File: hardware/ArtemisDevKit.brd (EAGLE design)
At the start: 94 x 38.1 mm, 228 parts, among them J2 CORTEX_JTAG_DEBUG_MINIMUM_PTH, J3 CORTEX_JTAG_DEBUG_PTH, J5 1X04_SMD_STRAIGHT_COMBO, J6 QWIIC_RIGHT_ANGLE, J7 CAMERA-HIMAX, J9 1X04_SMD_STRAIGHT_COMBO, U1 DAPLINK_KL26Z, U2 ARTEMIS_MODULESMD, U3 LIS2DH12, U4 AP2127K-1.8V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

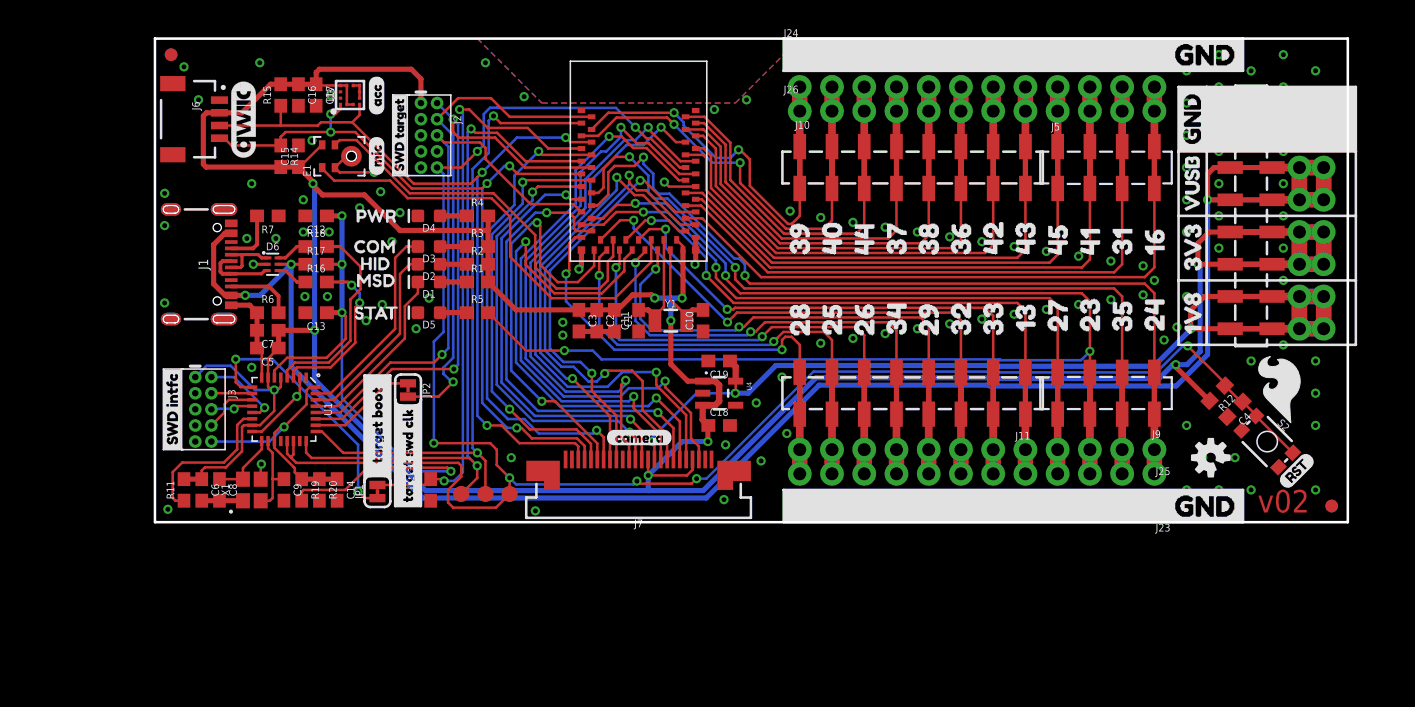
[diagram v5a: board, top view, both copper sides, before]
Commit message: final touches for review
- updated library in use for the interface chip
- mitered jumper labels
- approved / fixed all drc errors
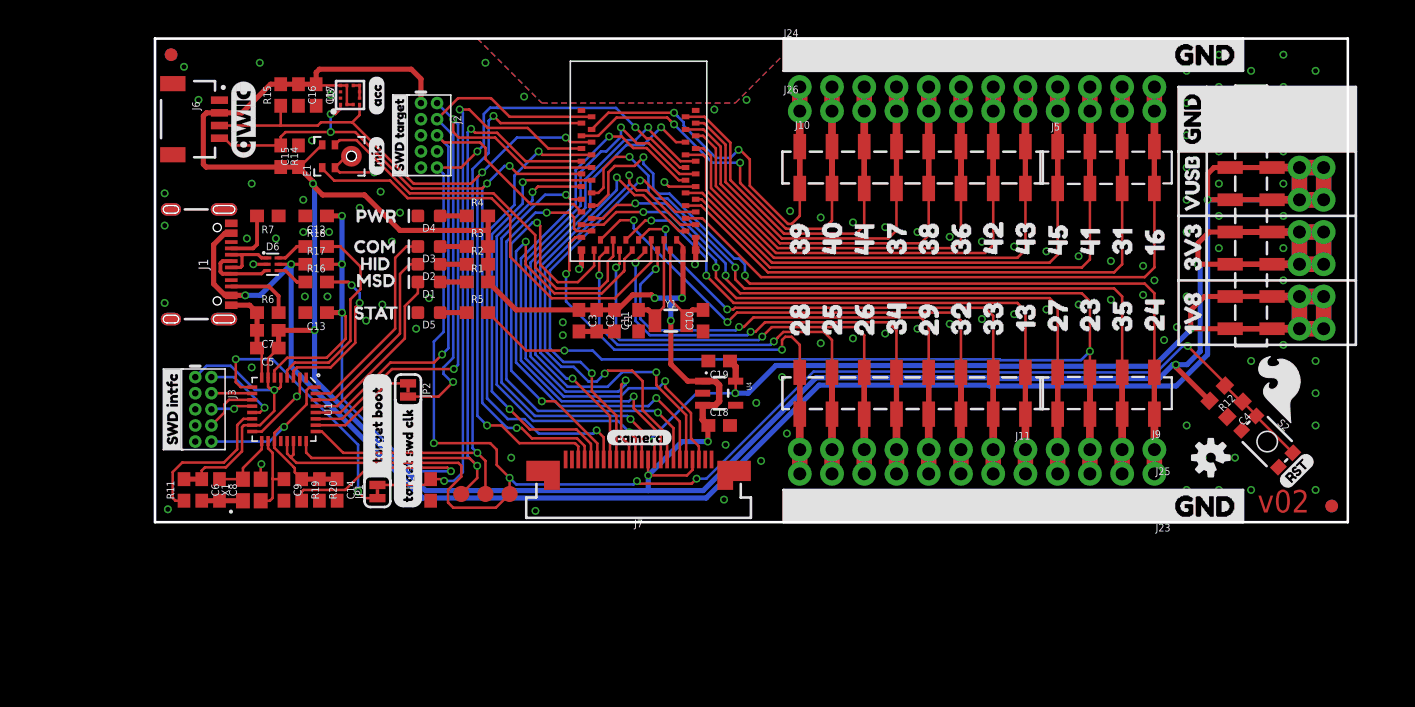
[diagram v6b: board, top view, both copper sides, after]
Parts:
- U1: device artembed:QFN-32-NOPAD -> ArtemisDevKit:QFN-32-NOPAD
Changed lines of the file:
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@@
 <layer number="37" name="tTest" color="7" fill="1" visible="no" active="yes"/>
 <layer number="38" name="bTest" color="7" fill="1" visible="no" active="yes"/>
-<layer number="39" name="tKeepout" color="4" fill="11" visible="no" active="yes"/>
-<layer number="40" name="bKeepout" color="1" fill="11" visible="no" active="yes"/>
+<layer number="39" name="tKeepout" color="4" fill="11" visible="yes" active="yes"/>
+<layer number="40" name="bKeepout" color="1" fill="11" visible="yes" active="yes"/>
 <layer number="41" name="tRestrict" color="4" fill="10" visible="no" active="yes"/>
 <layer number="42" name="bRestrict" color="1" fill="10" visible="no" active="yes"/>
@@
 <dimension x1="0" y1="38.1" x2="93.98" y2="38.1" x3="46.99" y3="44.45" textsize="1.778" textratio="15" layer="47" unit="inch"/>
 <text x="50.8" y="-13.335" size="1.778" layer="51" font="fixed" ratio="15">Owen Lyke, Kyle Wenner</text>
-<wire x1="16.51" y1="3.175" x2="16.51" y2="11.557" width="0.2032" layer="21"/>
-<wire x1="18.542" y1="11.557" x2="18.542" y2="2.921" width="0.2032" layer="21"/>
-<wire x1="18.542" y1="11.557" x2="16.51" y2="11.557" width="0.2032" layer="21"/>
-<wire x1="18.923" y1="9.652" x2="18.923" y2="1.27" width="0.2032" layer="21"/>
-<wire x1="18.923" y1="1.27" x2="20.955" y2="1.27" width="0.2032" layer="21"/>
-<wire x1="20.955" y1="1.27" x2="20.955" y2="9.652" width="0.2032" layer="21"/>
+<wire x1="17.145" y1="11.557" x2="17.907" y2="11.557" width="0.2032" layer="21"/>
+<wire x1="17.907" y1="11.557" x2="18.542" y2="10.922" width="0.2032" layer="21" curve="-90"/>
+<wire x1="18.542" y1="10.922" x2="18.542" y2="2.921" width="0.2032" layer="21"/>
+<wire x1="17.145" y1="11.557" x2="16.51" y2="10.922" width="0.2032" layer="21" curve="90"/>
+<wire x1="16.51" y1="10.922" x2="16.51" y2="3.175" width="0.2032" layer="21"/>
+<wire x1="18.923" y1="9.652" x2="18.923" y2="1.905" width="0.2032" layer="21"/>
+<wire x1="18.923" y1="1.905" x2="19.558" y2="1.27" width="0.2032" layer="21" curve="90"/>
+<wire x1="19.558" y1="1.27" x2="20.32" y2="1.27" width="0.2032" layer="21"/>
+<wire x1="20.32" y1="1.27" x2="20.955" y2="1.905" width="0.2032" layer="21" curve="90"/>
+<wire x1="20.955" y1="1.905" x2="20.955" y2="9.652" width="0.2032" layer="21"/>
 <rectangle x1="16.51" y1="4.191" x2="17.018" y2="10.922" layer="21"/>
 <rectangle x1="18.034" y1="4.191" x2="18.542" y2="10.922" layer="21"/>
-<rectangle x1="18.923" y1="1.27" x2="19.431" y2="9.271" layer="21"/>
-<rectangle x1="20.447" y1="1.27" x2="20.955" y2="9.271" layer="21"/>
 <rectangle x1="16.51" y1="3.556" x2="18.542" y2="4.445" layer="21"/>
-<rectangle x1="16.51" y1="10.795" x2="18.542" y2="11.557" layer="21"/>
+<rectangle x1="18.923" y1="1.524" x2="19.431" y2="9.271" layer="21"/>
+<rectangle x1="19.05" y1="1.397" x2="19.431" y2="1.651" layer="21"/>
+<rectangle x1="20.447" y1="1.397" x2="20.828" y2="1.651" layer="21"/>
+<rectangle x1="20.447" y1="1.524" x2="20.955" y2="9.271" layer="21"/>
+<rectangle x1="16.764" y1="10.795" x2="18.288" y2="11.557" layer="21"/>
+<rectangle x1="18.161" y1="10.922" x2="18.415" y2="11.43" layer="21"/>
+<rectangle x1="18.288" y1="10.795" x2="18.542" y2="11.303" layer="21"/>
+<rectangle x1="16.637" y1="10.795" x2="16.891" y2="11.43" layer="21"/>
+<rectangle x1="16.51" y1="10.795" x2="16.764" y2="11.176" layer="21"/>
 </plain>
 <attributes>
@@
 </class>
 </classes>
-<designrules name="SparkFun-2-layer-TIGHT">
+<designrules name="SparkFun-2-layer-FAB-LIMIT">
 <description language="en">&lt;b&gt;SparkFun 2 Layer Design Rule Checks - STANDARD/TIGHT/FAB-LIMIT&lt;/b&gt;
 &lt;p&gt;
@@
 <param name="mtCopper" value="0.035mm 0.035mm 0.035mm 0.035mm 0.035mm 0.035mm 0.035mm 0.035mm 0.035mm 0.035mm 0.035mm 0.035mm 0.035mm 0.035mm 0.035mm 0.035mm"/>
 <param name="mtIsolate" value="1.5mm 0.15mm 0.2mm 0.15mm 0.2mm 0.15mm 0.2mm 0.15mm 0.2mm 0.15mm 0.2mm 0.15mm 0.2mm 0.15mm 0.2mm"/>
-<param name="mdWireWire" value="7mil"/>
-<param name="mdWirePad" value="7mil"/>
-<param name="mdWireVia" value="7mil"/>
-<param name="mdPadPad" value="7mil"/>
-<param name="mdPadVia" value="7mil"/>
-<param name="mdViaVia" value="7mil"/>
-<param name="mdSmdPad" value="7mil"/>
-<param name="mdSmdVia" value="7mil"/>
-<param name="mdSmdSmd" value="7mil"/>
+<param name="mdWireWire" value="4mil"/>
+<param name="mdWirePad" value="4mil"/>
+<param name="mdWireVia" value="4mil"/>
+<param name="mdPadPad" value="4mil"/>
+<param name="mdPadVia" value="4mil"/>
+<param name="mdViaVia" value="4mil"/>
+<param name="mdSmdPad" value="4mil"/>
+<param name="mdSmdVia" value="4mil"/>
+<param name="mdSmdSmd" value="4mil"/>
 <param name="mdViaViaSameLayer" value="8mil"/>
 <param name="mnLayersViaInSmd" value="2"/>
-<param name="mdCopperDimension" value="7mil"/>
-<param name="mdDrill" value="7mil"/>
+<param name="mdCopperDimension" value="4mil"/>
+<param name="mdDrill" value="4mil"/>
 <param name="mdSmdStop" value="0mil"/>
-<param name="msWidth" value="7mil"/>
-<param name="msDrill" value="15mil"/>
+<param name="msWidth" value="4mil"/>
+<param name="msDrill" value="6mil"/>
 <param name="msMicroVia" value="9.99mm"/>
 <param name="msBlindViaRatio" value="0.5"/>
@@
 <param name="rvMicroViaOuter" value="0.25"/>
 <param name="rvMicroViaInner" value="0.25"/>
-<param name="rlMinPadTop" value="7mil"/>
+<param name="rlMinPadTop" value="5mil"/>
 <param name="rlMaxPadTop" value="20mil"/>
-<param name="rlMinPadInner" value="7mil"/>
+<param name="rlMinPadInner" value="6mil"/>
 <param name="rlMaxPadInner" value="20mil"/>
-<param name="rlMinPadBottom" value="7mil"/>
+<param name="rlMinPadBottom" value="5mil"/>
 <param name="rlMaxPadBottom" value="20mil"/>
-<param name="rlMinViaOuter" value="7mil"/>
+<param name="rlMinViaOuter" value="5mil"/>
 <param name="rlMaxViaOuter" value="20mil"/>
-<param name="rlMinViaInner" value="7mil"/>
+<param name="rlMinViaInner" value="6mil"/>
 <param name="rlMaxViaInner" value="20mil"/>
 <param name="rlMinMicroViaOuter" value="4mil"/>
@@
 <element name="TP3" library="SparkFun-Connectors" package="PAD.03X.05" value="TEST-POINT3X5" x="24.13" y="2.2225" smashed="yes"/>
 <element name="TP4" library="SparkFun-Connectors" package="PAD.03X.05" value="TEST-POINT3X5" x="26.035" y="2.2225" smashed="yes"/>
-<element name="U1" library="artembed" package="QFN-32-NOPAD" value="DAPLINK_KL26Z" x="10.16" y="8.89" smashed="yes" rot="R180">
+<element name="U1" library="ArtemisDevKit" package="QFN-32-NOPAD" value="DAPLINK_KL26Z" x="10.16" y="8.89" smashed="yes" rot="R180">
 <attribute name="NAME" x="13.335" y="8.89" size="0.6096" layer="25" font="vector" ratio="20" rot="R270" align="bottom-center"/>
 <attribute name="VALUE" x="6.35" y="8.89" size="0.6096" layer="27" font="vector" ratio="20" rot="R270" align="bottom-center"/>
@@
 <wire x1="25.2147" y1="30.678" x2="26.95481875" y2="30.678" width="0.2032" layer="1"/>
 <wire x1="26.95481875" y1="30.678" x2="29.19281875" y2="28.44" width="0.2032" layer="1"/>
-<wire x1="24.13" y1="2.2225" x2="24.1046" y2="2.2479" width="0.2032" layer="1"/>
 <wire x1="24.638" y1="30.7213" x2="24.638" y2="5.1943" width="0.2032" layer="16"/>
 <wire x1="24.638" y1="5.1943" x2="25.3873" y2="4.445" width="0.2032" layer="16"/>
@@
 <wire x1="26.218" y1="31.059" x2="24.765" y2="32.512" width="0.2032" layer="1"/>
 <wire x1="24.765" y1="32.512" x2="24.003" y2="32.512" width="0.2032" layer="1"/>
-<wire x1="17.5387" y1="2.921" x2="17.526" y2="2.9337" width="0.2032" layer="1"/>
 <via x="22.7838" y="3.2512" extent="1-16" drill="0.381"/>
 <wire x1="24.257" y1="32.258" x2="24.257" y2="3.937" width="0.2032" layer="16"/>

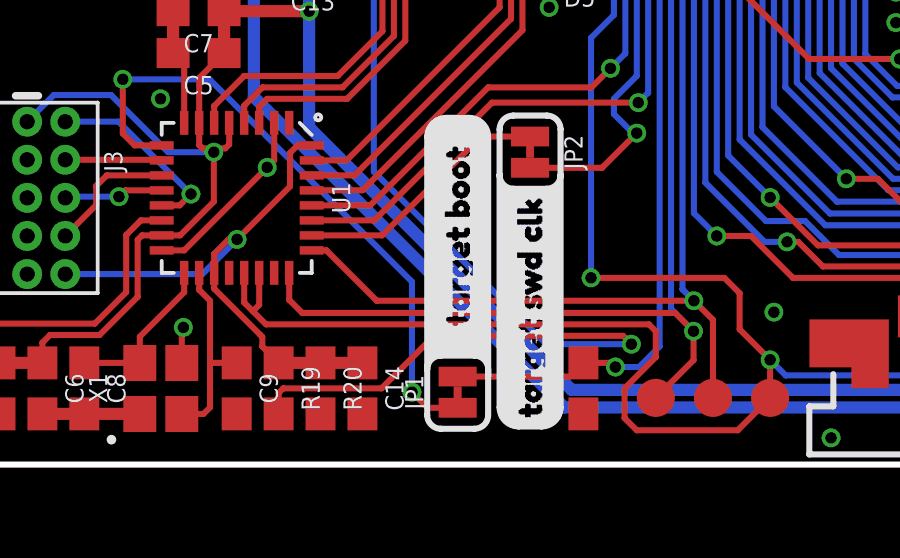
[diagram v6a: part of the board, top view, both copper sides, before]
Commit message: rework TGT_RST routing
just a minor optimization
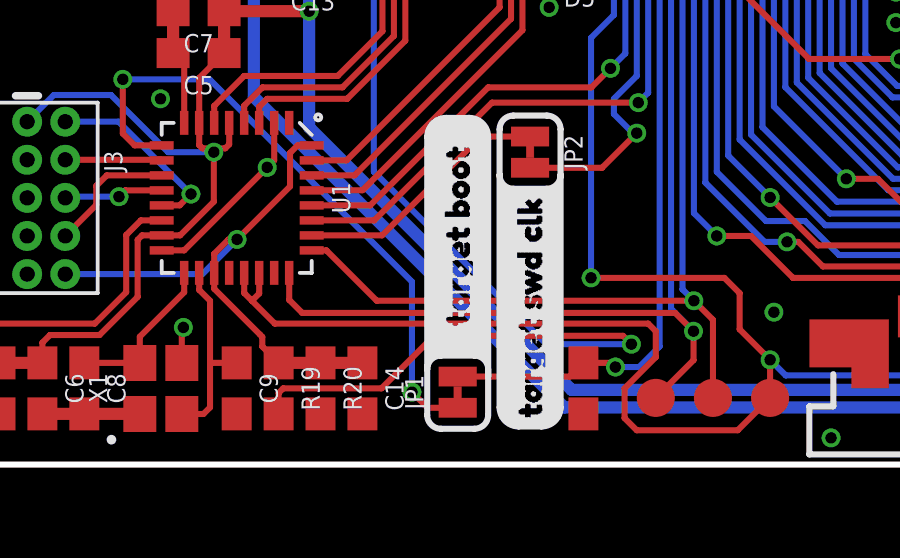
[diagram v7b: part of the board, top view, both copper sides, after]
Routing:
- net !TGT_RST: track 151.9 -> 151.4 mm
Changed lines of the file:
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@@
 <wire x1="26.416" y1="6.223" x2="21.971" y2="6.223" width="0.2032" layer="1"/>
 <wire x1="24.13" y1="3.5814" x2="23.0886" y2="2.54" width="0.2032" layer="1"/>
-<wire x1="24.13" y1="4.445" x2="24.13" y2="3.5814" width="0.2032" layer="1"/>
-<wire x1="11.1360375" y1="4.6736" x2="23.9014" y2="4.6736" width="0.2032" layer="1"/>
-<wire x1="23.9014" y1="4.6736" x2="24.13" y2="4.445" width="0.2032" layer="1"/>
+<wire x1="24.13" y1="3.5814" x2="24.13" y2="4.445" width="0.2032" layer="1"/>
 <contactref element="U1" pad="21"/>
-<wire x1="10.41" y1="6.39" x2="10.41" y2="5.3996375" width="0.2032" layer="1"/>
-<wire x1="10.41" y1="5.3996375" x2="10.69881875" y2="5.11081875" width="0.2032" layer="1"/>
-<wire x1="10.69881875" y1="5.11081875" x2="11.1360375" y2="4.6736" width="0.2032" layer="1"/>
-<wire x1="10.91" y1="6.39" x2="10.91" y2="5.322" width="0.2032" layer="1"/>
-<wire x1="10.91" y1="5.322" x2="10.69881875" y2="5.11081875" width="0.2032" layer="1"/>
+<wire x1="10.41" y1="5.719" x2="10.41" y2="6.39" width="0.2032" layer="1"/>
+<wire x1="24.13" y1="4.445" x2="23.876" y2="4.699" width="0.2032" layer="1"/>
+<wire x1="23.876" y1="4.699" x2="11.43" y2="4.699" width="0.2032" layer="1"/>
+<wire x1="11.43" y1="4.699" x2="10.668" y2="5.461" width="0.2032" layer="1"/>
+<wire x1="10.668" y1="5.461" x2="10.41" y2="5.719" width="0.2032" layer="1"/>
+<wire x1="10.91" y1="6.39" x2="10.91" y2="5.703" width="0.2032" layer="1"/>
+<wire x1="10.91" y1="5.703" x2="10.668" y2="5.461" width="0.2032" layer="1"/>
 </signal>
 <signal name="N$14">
